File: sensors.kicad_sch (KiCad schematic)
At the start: 13 parts, among them J2 Conn_Coaxial, U14 ISM6HG256X, U18 LIS2MDL, U3 MS5607-02BA, U5 MAX-M10S

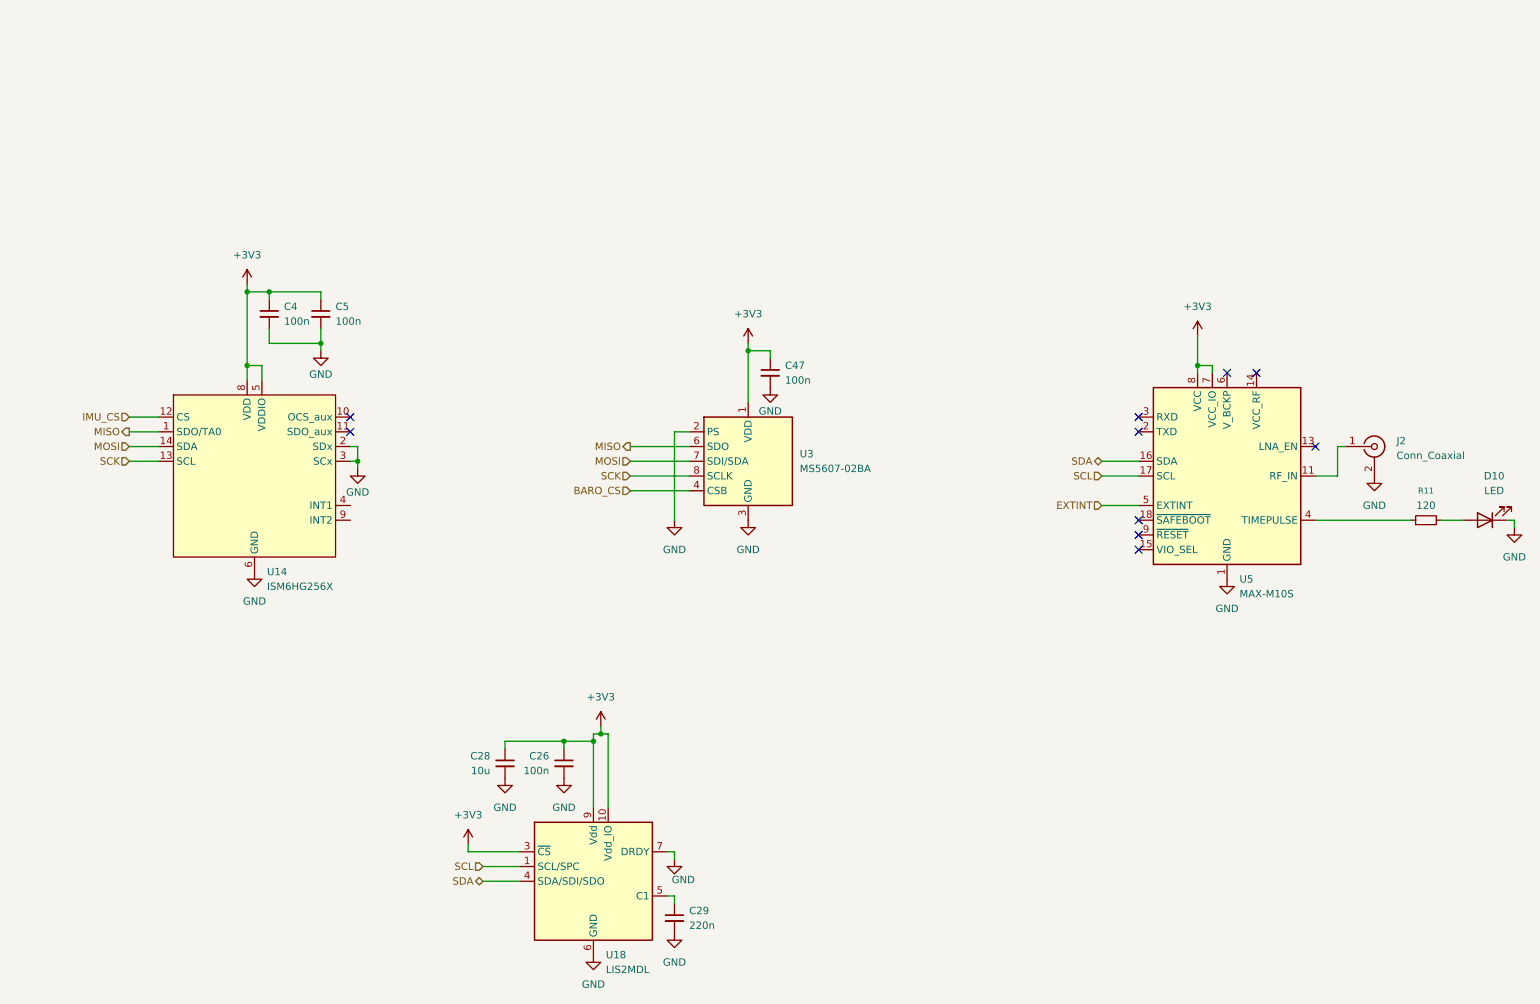
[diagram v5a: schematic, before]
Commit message: switched to global labels for SPI and I2C, added labels for servos
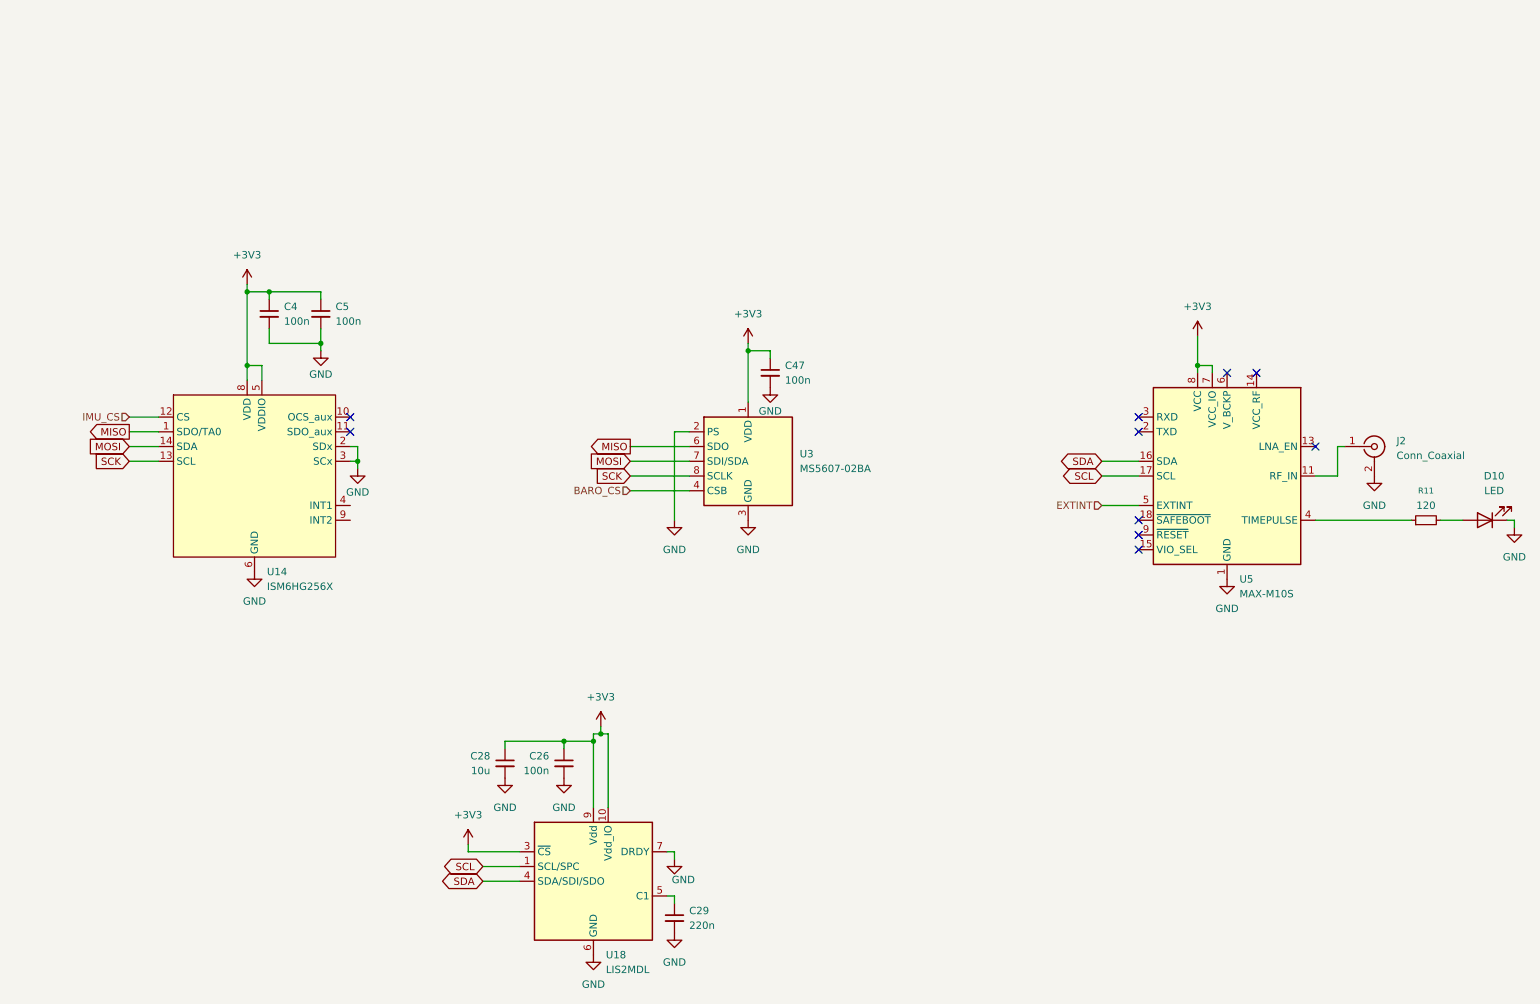
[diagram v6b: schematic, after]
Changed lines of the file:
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@@
 		)
 	)
-	(hierarchical_label "IMU_CS"
-		(shape input)
-		(at 41.91 92.71 180)
-		(effects
-			(font
-				(size 1.27 1.27)
-			)
-			(justify right)
-		)
-	)
-	(hierarchical_label "SCL"
-		(shape input)
-		(at 209.55 102.87 180)
-		(effects
-			(font
-				(size 1.27 1.27)
-			)
-			(justify right)
-		)
-	)
-	(hierarchical_label "SCL"
-		(shape input)
-		(at 102.87 170.18 180)
-		(effects
-			(font
-				(size 1.27 1.27)
-			)
-			(justify right)
-		)
-	)
-	(hierarchical_label "SCK"
+	(global_label "SCK"
 		(shape input)
 		(at 128.27 102.87 180)
-		(effects
-			(font
-				(size 1.27 1.27)
-			)
-			(justify right)
-		)
-	)
-	(hierarchical_label "MISO"
+		(fields_autoplaced yes)
+		(effects
+			(font
+				(size 1.27 1.27)
+			)
+			(justify right)
+		)
+		(property "Intersheetrefs" "${INTERSHEET_REFS}"
+			(at 121.5353 102.87 0)
+			(effects
+				(font
+					(size 1.27 1.27)
+				)
+				(justify right)
+				(hide yes)
+			)
+		)
+	)
+	(global_label "SDA"
+		(shape bidirectional)
+		(at 209.55 100.33 180)
+		(fields_autoplaced yes)
+		(effects
+			(font
+				(size 1.27 1.27)
+			)
+			(justify right)
+		)
+		(property "Intersheetrefs" "${INTERSHEET_REFS}"
+			(at 201.8854 100.33 0)
+			(effects
+				(font
+					(size 1.27 1.27)
+				)
+				(justify right)
+				(hide yes)
+			)
+		)
+	)
+	(global_label "MOSI"
+		(shape input)
+		(at 41.91 97.79 180)
+		(fields_autoplaced yes)
+		(effects
+			(font
+				(size 1.27 1.27)
+			)
+			(justify right)
+		)
+		(property "Intersheetrefs" "${INTERSHEET_REFS}"
+			(at 34.3286 97.79 0)
+			(effects
+				(font
+					(size 1.27 1.27)
+				)
+				(justify right)
+				(hide yes)
+			)
+		)
+	)
+	(global_label "MISO"
 		(shape output)
 		(at 128.27 97.79 180)
-		(effects
-			(font
-				(size 1.27 1.27)
-			)
-			(justify right)
-		)
-	)
-	(hierarchical_label "MOSI"
+		(fields_autoplaced yes)
+		(effects
+			(font
+				(size 1.27 1.27)
+			)
+			(justify right)
+		)
+		(property "Intersheetrefs" "${INTERSHEET_REFS}"
+			(at 120.6886 97.79 0)
+			(effects
+				(font
+					(size 1.27 1.27)
+				)
+				(justify right)
+				(hide yes)
+			)
+		)
+	)
+	(global_label "SCK"
+		(shape input)
+		(at 41.91 100.33 180)
+		(fields_autoplaced yes)
+		(effects
+			(font
+				(size 1.27 1.27)
+			)
+			(justify right)
+		)
+		(property "Intersheetrefs" "${INTERSHEET_REFS}"
+			(at 35.1753 100.33 0)
+			(effects
+				(font
+					(size 1.27 1.27)
+				)
+				(justify right)
+				(hide yes)
+			)
+		)
+	)
+	(global_label "SCL"
+		(shape bidirectional)
+		(at 209.55 102.87 180)
+		(fields_autoplaced yes)
+		(effects
+			(font
+				(size 1.27 1.27)
+			)
+			(justify right)
+		)
+		(property "Intersheetrefs" "${INTERSHEET_REFS}"
+			(at 201.9459 102.87 0)
+			(effects
+				(font
+					(size 1.27 1.27)
+				)
+				(justify right)
+				(hide yes)
+			)
+		)
+	)
+	(global_label "MOSI"
 		(shape input)
 		(at 128.27 100.33 180)
-		(effects
-			(font
-				(size 1.27 1.27)
-			)
-			(justify right)
-		)
-	)
-	(hierarchical_label "MOSI"
-		(shape input)
-		(at 41.91 97.79 180)
-		(effects
-			(font
-				(size 1.27 1.27)
-			)
-			(justify right)
-		)
-	)
-	(hierarchical_label "MISO"
+		(fields_autoplaced yes)
+		(effects
+			(font
+				(size 1.27 1.27)
+			)
+			(justify right)
+		)
+		(property "Intersheetrefs" "${INTERSHEET_REFS}"
+			(at 120.6886 100.33 0)
+			(effects
+				(font
+					(size 1.27 1.27)
+				)
+				(justify right)
+				(hide yes)
+			)
+		)
+	)
+	(global_label "MISO"
 		(shape output)
 		(at 41.91 95.25 180)
-		(effects
-			(font
-				(size 1.27 1.27)
-			)
-			(justify right)
-		)
-	)
-	(hierarchical_label "SDA"
-		(shape bidirectional)
-		(at 209.55 100.33 180)
-		(effects
-			(font
-				(size 1.27 1.27)
-			)
-			(justify right)
-		)
-	)
-	(hierarchical_label "SCK"
-		(shape input)
-		(at 41.91 100.33 180)
+		(fields_autoplaced yes)
+		(effects
+			(font
+				(size 1.27 1.27)
+			)
+			(justify right)
+		)
+		(property "Intersheetrefs" "${INTERSHEET_REFS}"
+			(at 34.3286 95.25 0)
+			(effects
+				(font
+					(size 1.27 1.27)
+				)
+				(justify right)
+				(hide yes)
+			)
+		)
+	)
+	(global_label "SCL"
+		(shape bidirectional)
+		(at 102.87 170.18 180)
+		(fields_autoplaced yes)
+		(effects
+			(font
+				(size 1.27 1.27)
+			)
+			(justify right)
+		)
+		(property "Intersheetrefs" "${INTERSHEET_REFS}"
+			(at 95.2659 170.18 0)
+			(effects
+				(font
+					(size 1.27 1.27)
+				)
+				(justify right)
+				(hide yes)
+			)
+		)
+	)
+	(global_label "SDA"
+		(shape bidirectional)
+		(at 102.87 172.72 180)
+		(fields_autoplaced yes)
+		(effects
+			(font
+				(size 1.27 1.27)
+			)
+			(justify right)
+		)
+		(property "Intersheetrefs" "${INTERSHEET_REFS}"
+			(at 95.2054 172.72 0)
+			(effects
+				(font
+					(size 1.27 1.27)
+				)
+				(justify right)
+				(hide yes)
+			)
+		)
+	)
+	(hierarchical_label "IMU_CS"
+		(shape input)
+		(at 41.91 92.71 180)
 		(effects
 			(font
@@
 		(effects
 			(font
-				(size 1.27 1.27)
-			)
-			(justify right)
-		)
-	)
-	(hierarchical_label "SDA"
-		(shape bidirectional)
-		(at 102.87 172.72 180)
-		(effects
-			(font

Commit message: various tweaks
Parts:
- R11: value 120 -> 1k; LCSC C25077 -> C11702
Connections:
- net at U5.4 (TIMEPULSE): now also R11.2; no longer R11.1
- net at D10.2 (A): now also R11.1; no longer R11.2
- no-connect marks 10 -> 12
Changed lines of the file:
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@@
 	)
 	(no_connect
+		(at 80.01 107.95)
+	)
+	(no_connect
 		(at 215.9 92.71)
 	)
@@
 	)
 	(no_connect
+		(at 80.01 110.49)
+	)
+	(no_connect
 		(at 80.01 92.71)
 	)
@@
 	)
 	(symbol
+		(lib_id "Device:R_Small")
+		(at 265.43 110.49 270)
+		(unit 1)
+		(exclude_from_sim no)
+		(in_bom yes)
+		(on_board yes)
+		(dnp no)
+		(property "Reference" "R11"
+			(at 265.43 105.41 90)
+			(effects
+				(font
+					(size 1.016 1.016)
+				)
+			)
+		)
+		(property "Value" "1k"
+			(at 265.43 107.95 90)
+			(effects
+				(font
+					(size 1.27 1.27)
+				)
+			)
+		)
+		(property "Footprint" "Resistor_SMD:R_0402_1005Metric"
+			(at 265.43 110.49 0)
+			(effects
+				(font
+					(size 1.27 1.27)
+				)
+				(hide yes)
+			)
+		)
+		(property "Datasheet" "~"
+			(at 265.43 110.49 0)
+			(effects
+				(font
+					(size 1.27 1.27)
+				)
+				(hide yes)
+			)
+		)
+		(property "Description" "Resistor, small symbol"
+			(at 265.43 110.49 0)
+			(effects
+				(font
+					(size 1.27 1.27)
+				)
+				(hide yes)
+			)
+		)
+		(property "LCSC" "C11702"
+			(at 265.43 110.49 90)
+			(effects
+				(font
+					(size 1.27 1.27)
+				)
+				(hide yes)
+			)
+		)
+		(property "digikey" ""
+			(at 265.43 110.49 90)
+			(effects
+				(font
+					(size 1.27 1.27)
+				)
+				(hide yes)
+			)
+		)
+		(pin "1"
+		)
+		(pin "2"
+		)
+		(instances
+			(project "beavs-sketch-0"
+				(path "/49232f62-a438-4b3e-9be5-c2b3074d8de1/c418f66a-3bfd-48e4-bf5e-1b050c211ac2"
+					(reference "R11")
+					(unit 1)
+				)
+			)
+		)
+	)
+	(symbol
 		(lib_id "power:GND")
 		(at 280.67 111.76 0)
@@
 					(unit 1)
 				)
-			)
-		)
-	)
-	(symbol
-		(lib_id "Device:R_Small")
-		(at 265.43 110.49 90)
-		(unit 1)
-		(exclude_from_sim no)
-		(in_bom yes)
-		(on_board yes)
-		(dnp no)
-		(fields_autoplaced yes)
-		(property "Reference" "R11"
-			(at 265.43 105.41 90)
-			(effects
-				(font
-					(size 1.016 1.016)
-				)
-			)
-		)
-		(property "Value" "120"
-			(at 265.43 107.95 90)
-			(effects
-				(font
-					(size 1.27 1.27)
-				)
-			)
-		)
-		(property "Footprint" "Resistor_SMD:R_0402_1005Metric"
-			(at 265.43 110.49 0)
-			(effects
-				(font
-					(size 1.27 1.27)
-				)
-				(hide yes)
-			)
-		)
-		(property "Datasheet" "~"
-			(at 265.43 110.49 0)
-			(effects
-				(font
-					(size 1.27 1.27)
-				)
-				(hide yes)
-			)
-		)
-		(property "Description" "Resistor, small symbol"
-			(at 265.43 110.49 0)
-			(effects
-				(font
-					(size 1.27 1.27)
-				)
-				(hide yes)
-			)
-		)
-		(property "LCSC" "C25077"
-			(at 265.43 110.49 90)
-			(effects
-				(font
-					(size 1.27 1.27)
-				)
-				(hide yes)
-			)
-		)
-		(property "digikey" ""
-			(at 265.43 110.49 90)
-			(effects
-				(font
-					(size 1.27 1.27)
-				)
-				(hide yes)
-			)
-		)
-		(pin "1"
-		)
-		(pin "2"
-		)
-		(instances
-			(project ""
-				(path "/49232f62-a438-4b3e-9be5-c2b3074d8de1/c418f66a-3bfd-48e4-bf5e-1b050c211ac2"
-					(reference "R11")
-					(unit 1)
-				)

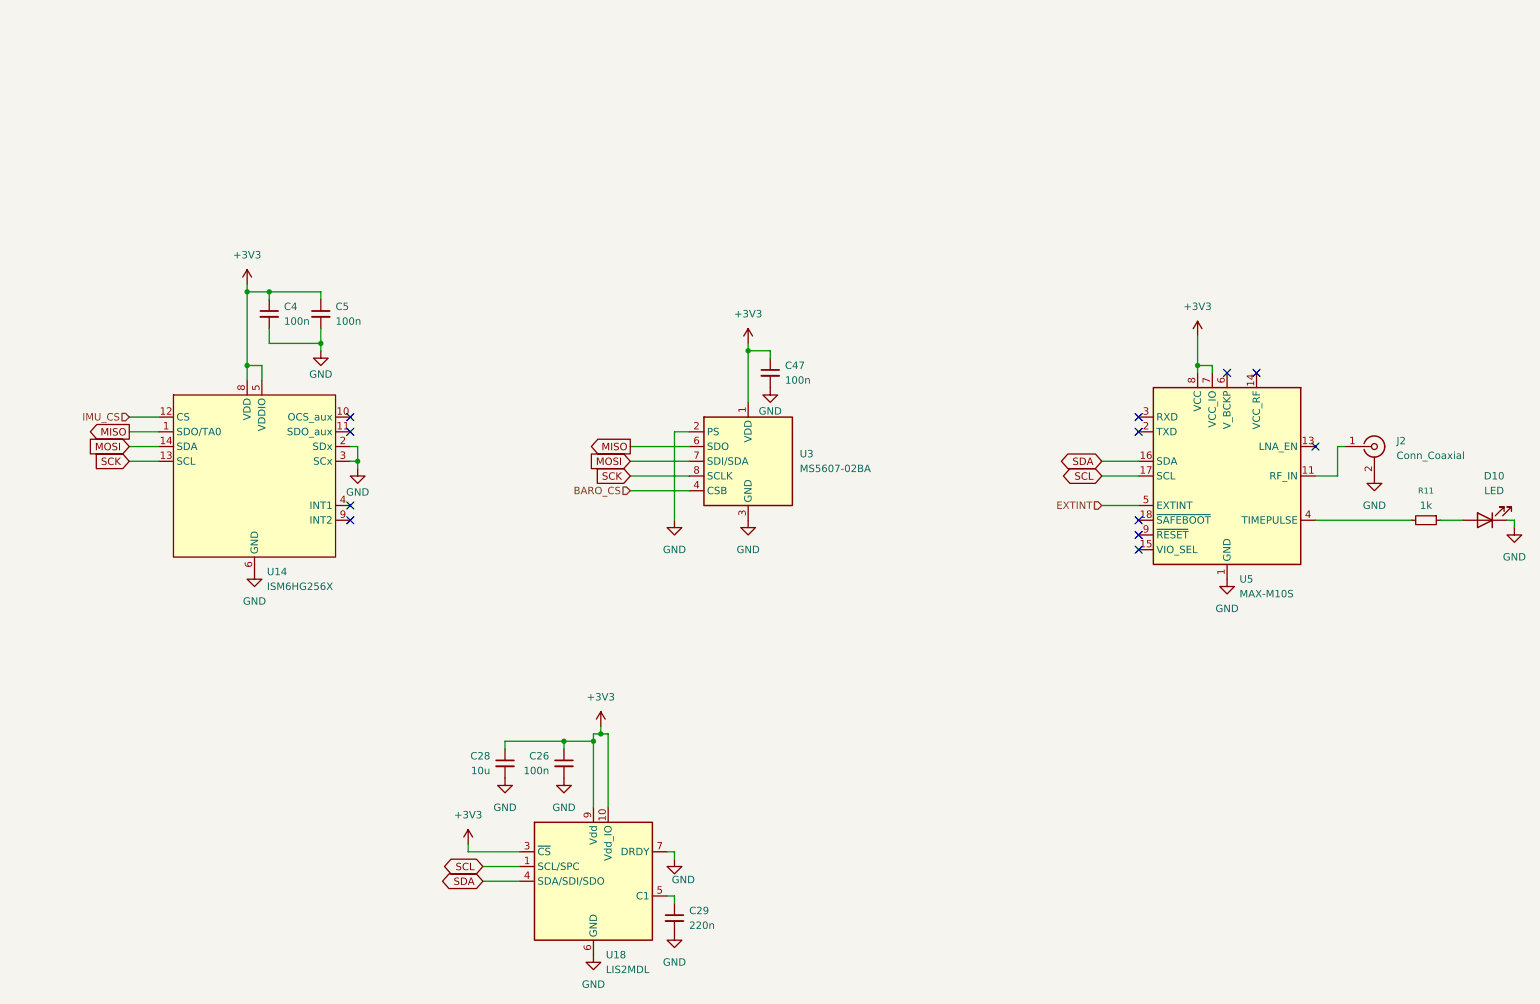
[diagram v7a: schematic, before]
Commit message: add schematic PDF, improve schematic readability
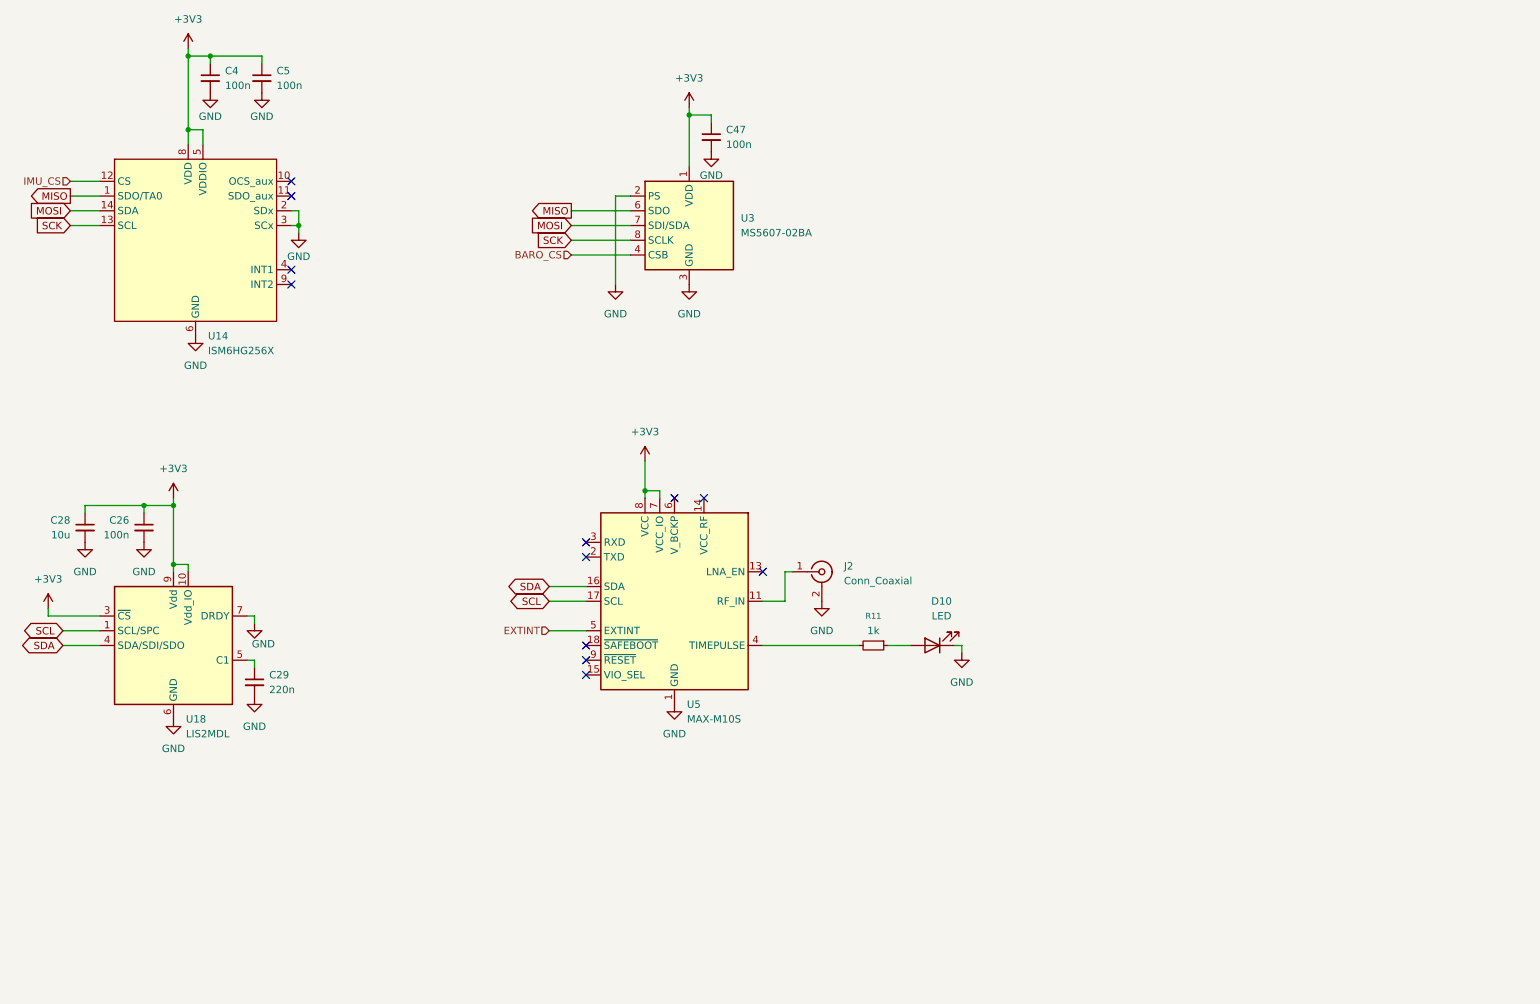
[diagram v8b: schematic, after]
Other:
- moved on the sheet: C26, C28, C29, C4, C47, C5, D10, J2, R11, U14, U18, U3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
